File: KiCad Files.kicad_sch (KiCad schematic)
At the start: 4 parts, among them J1 Power, J2 Digital/PWM, J3 Analog, J4 Digital/PWM

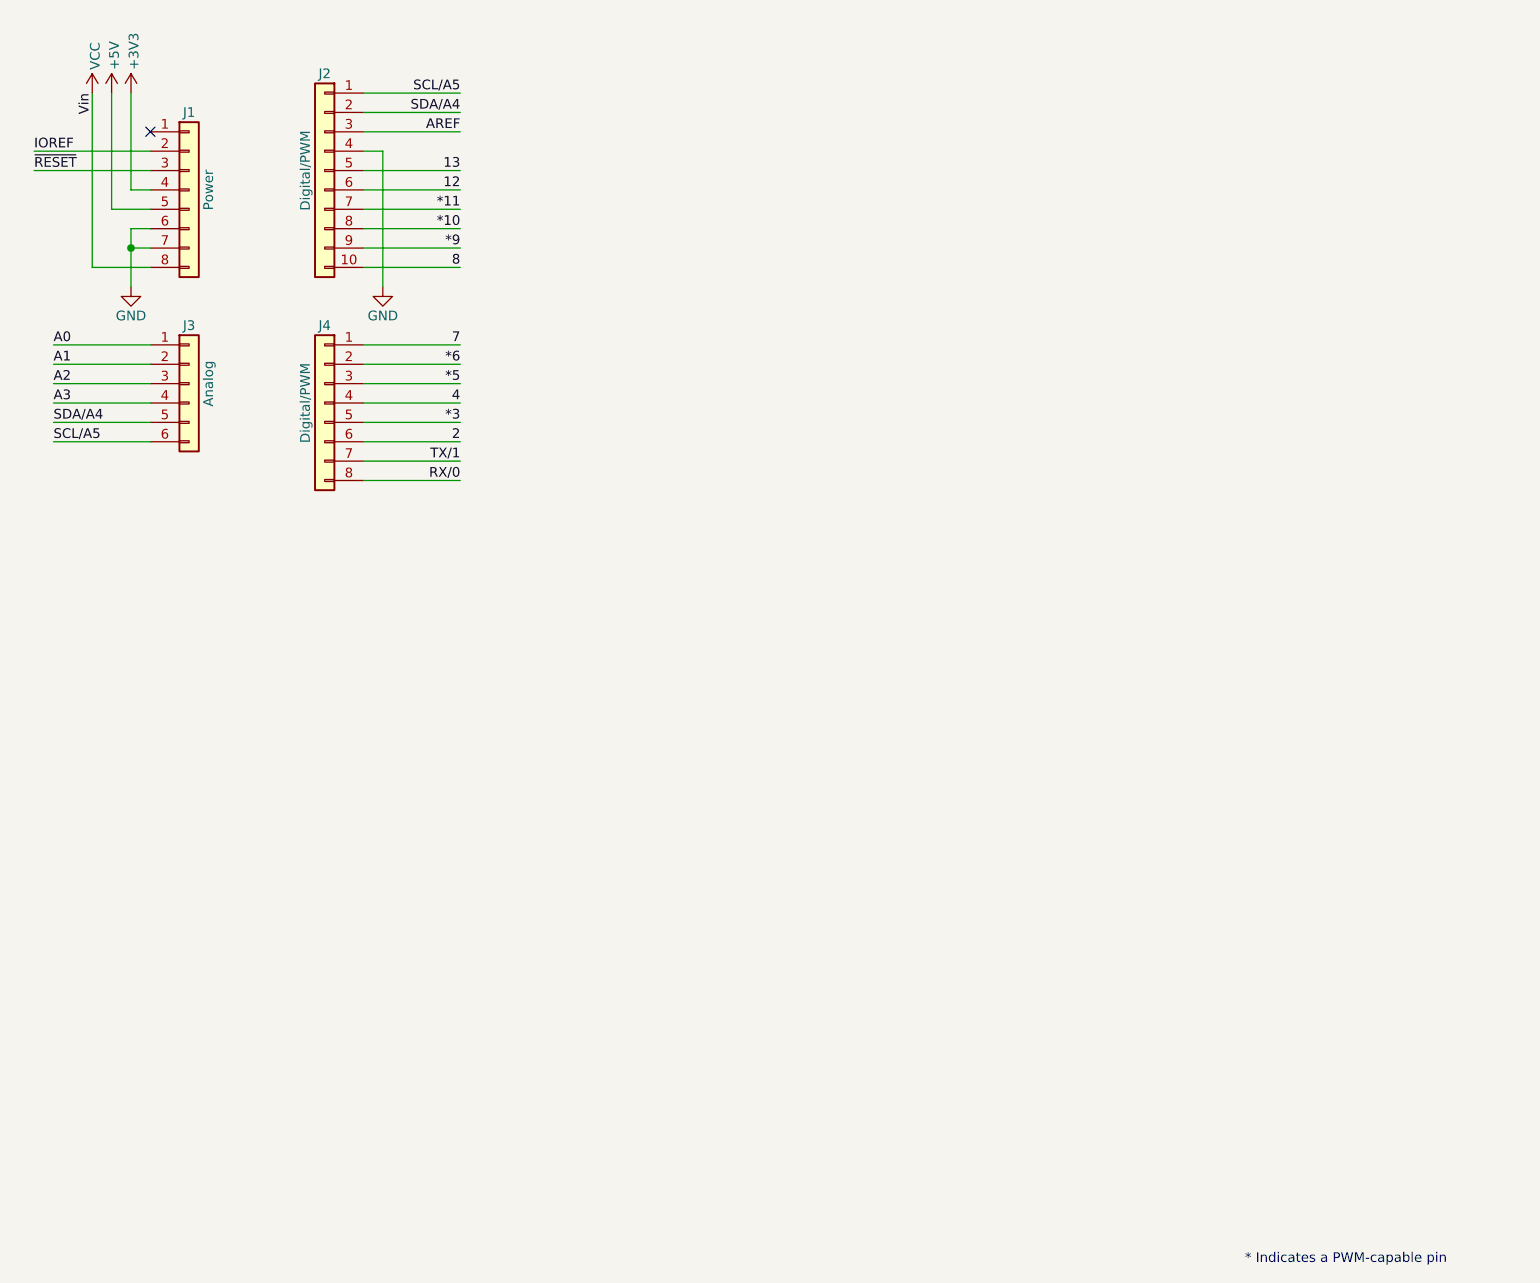
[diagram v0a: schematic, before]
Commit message: Added Connections to BME680
Configured based on datasheet for 12C communication protocol.
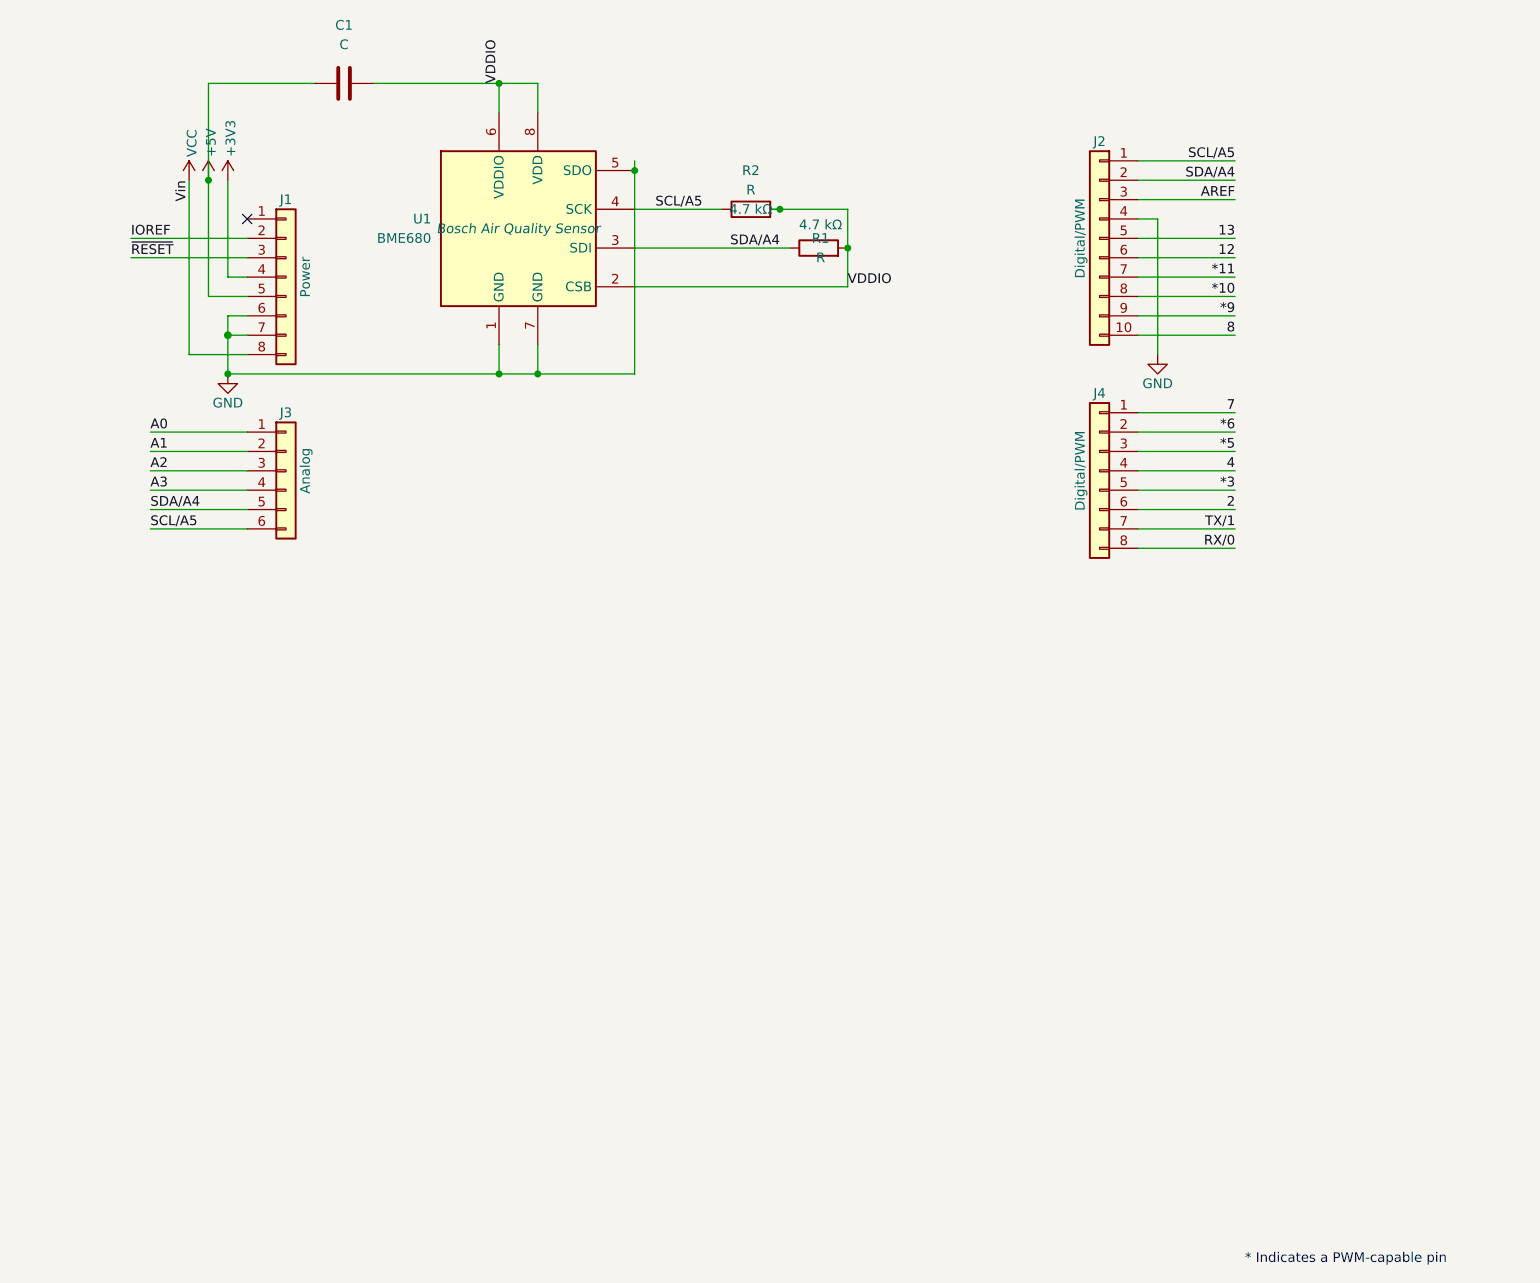
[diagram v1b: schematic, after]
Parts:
- added C1: C, Capacitor_THT:C_Axial_L3.8mm_D2.6mm_P7.50mm_Horizontal, symbol Device:C
- added R1: R, Resistor_THT:R_Axial_DIN0204_L3.6mm_D1.6mm_P1.90mm_Vertical, symbol Device:R
- added R2: R, symbol Device:R
- added U1: BME680, Package_LGA:Bosch_LGA-8_3x3mm_P0.8mm_ClockwisePinNumbering, symbol Sensor:BME680
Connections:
- net +5V: now also C1.2
- net GND: now also U1.1 (GND), U1.5 (SDO), U1.7 (GND)
- net SCL/A5: now also R2.1, U1.4 (SCK)
- net SDA/A4: now also R1.1, U1.3 (SDI)
- new net VDDIO: C1.1, R1.2, R2.2, U1.2 (CSB), U1.6 (VDDIO), U1.8 (VDD)
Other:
- moved on the sheet: J1, J2, J3, J4

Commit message: Added SHT30 Part and Connections
Added labels.
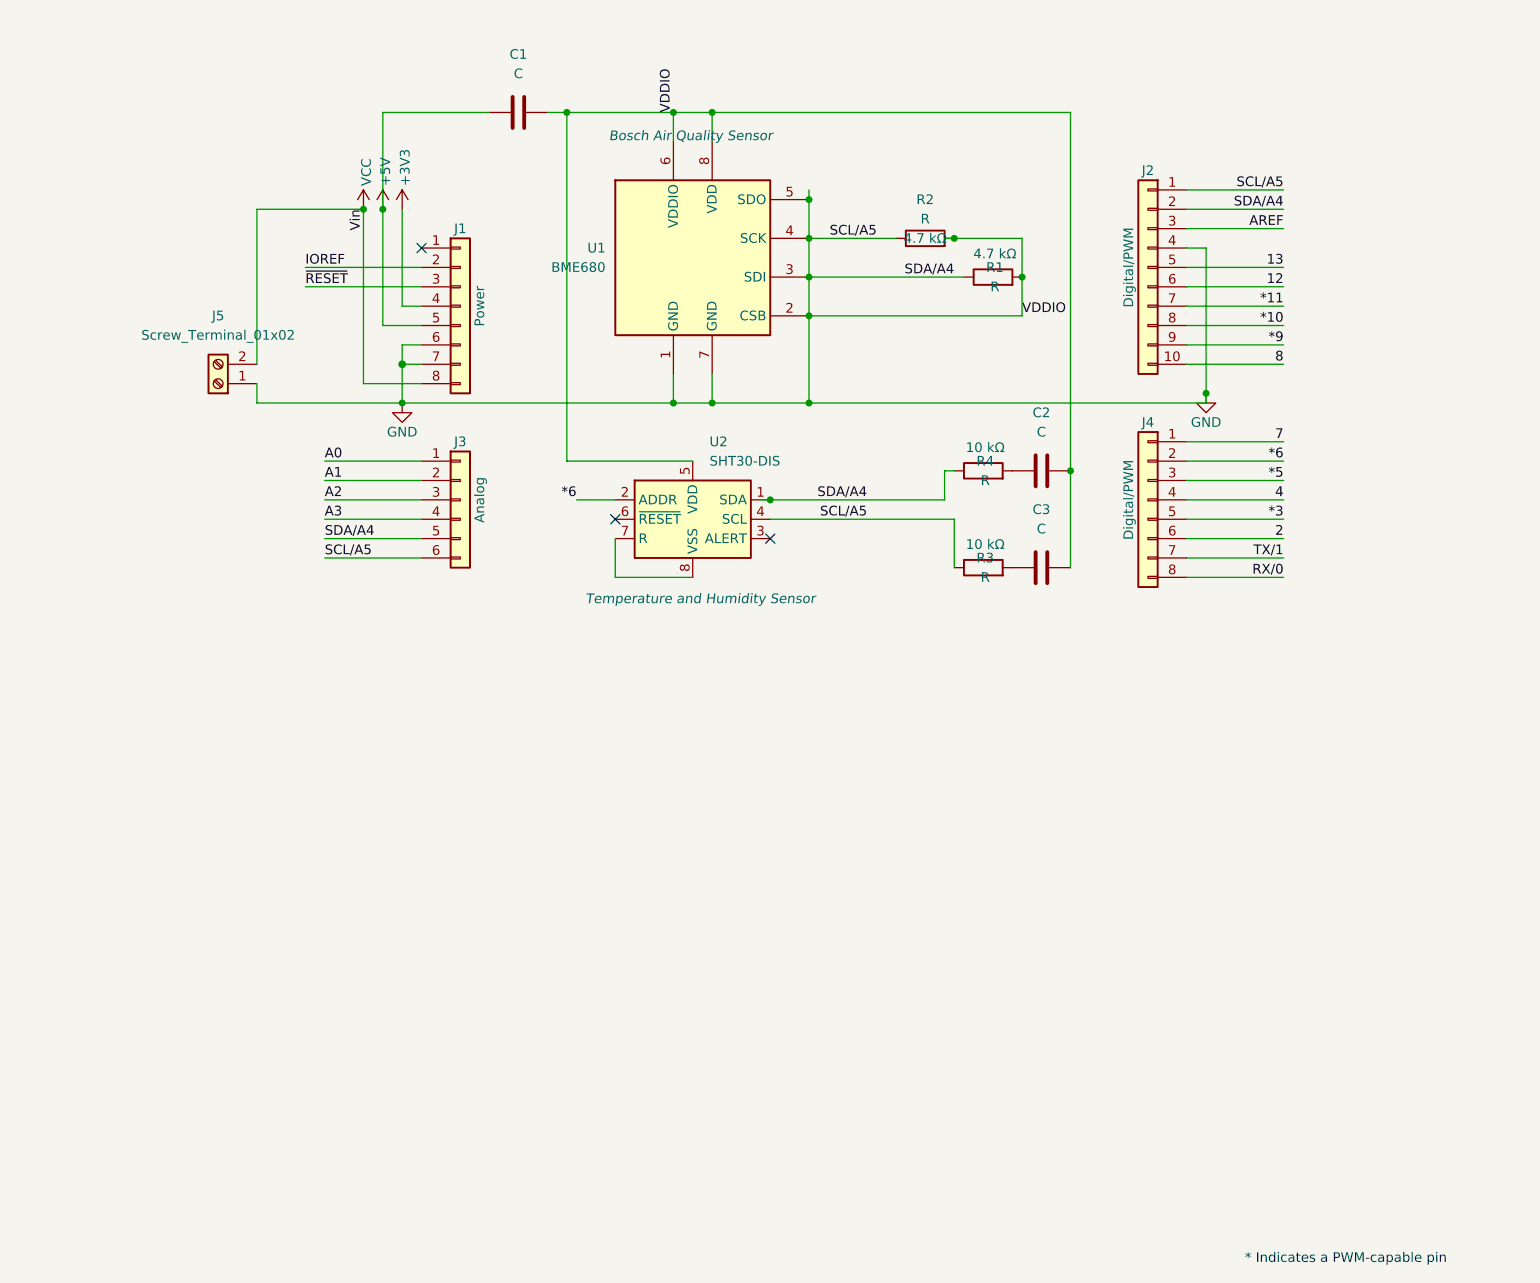
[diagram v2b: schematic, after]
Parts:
- added C2, C3: C, Capacitor_THT:C_Axial_L3.8mm_D2.6mm_P7.50mm_Horizontal, symbol Device:C
- added J5: Screw_Terminal_01x02, symbol Connector:Screw_Terminal_01x02
- added R3, R4: R, Resistor_THT:R_Axial_DIN0204_L3.6mm_D1.6mm_P1.90mm_Vertical, symbol Device:R
- added U2: SHT30-DIS, Sensor_Humidity:Sensirion_DFN-8-1EP_2.5x2.5mm_P0.5mm_EP1.1x1.7mm, symbol Sensor_Humidity:SHT30-DIS
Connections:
- net SCL/A5 is gone; now on net GND: J2.1 (Pin_1), J3.6 (Pin_6), R2.1, U1.4 (SCK)
- net SDA/A4 is gone; now on net GND: J2.2 (Pin_2), J3.5 (Pin_5), R1.1, U1.3 (SDI)
- net VDDIO is gone; now on net GND: C1.1, R1.2, R2.2, U1.2 (CSB), U1.6 (VDDIO), U1.8 (VDD)
- net *6: now also U2.2 (ADDR)
- net GND: now also C2.1, C3.1, J5.1 (Pin_1), R3.1, R4.1, U2.1 (SDA), U2.4 (SCL), U2.5 (VDD)
- net VCC: now also J5.2 (Pin_2)
- new net: C2.2, R4.2
- new net: U2.7 (R), U2.8 (VSS), U2.9 (VSS)
- new net: C3.2, R3.2
- no-connect marks 1 -> 3
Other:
- moved on the sheet: C1, J1, J2, J3, J4, R1, R2, U1

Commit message: FinalSchematicPDF Added
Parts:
- J5: footprint (none) -> TerminalBlock:TerminalBlock_Xinya_XY308-2.54-2P_1x02_P2.54mm_Horizontal
- R2: footprint (none) -> Resistor_THT:R_Axial_DIN0204_L3.6mm_D1.6mm_P1.90mm_Vertical
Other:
- moved on the sheet: C1, C2, C3, J1, J2, J3, J4, J5, R1, R2, R3, R4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
